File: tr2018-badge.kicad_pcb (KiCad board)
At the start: 2 copper layers, 70.4 x 53.3 mm, 23 parts, among them J1 Conn_01x02, J2 Conn_01x02, SW1 SW_SPDT, SW3 SW_Push, SW4 SW_Push, SW5 (opt.) SW_SPDT, U1 ESP-12F (opt.), X1 Defcon Shitty AddOn (opt.) >

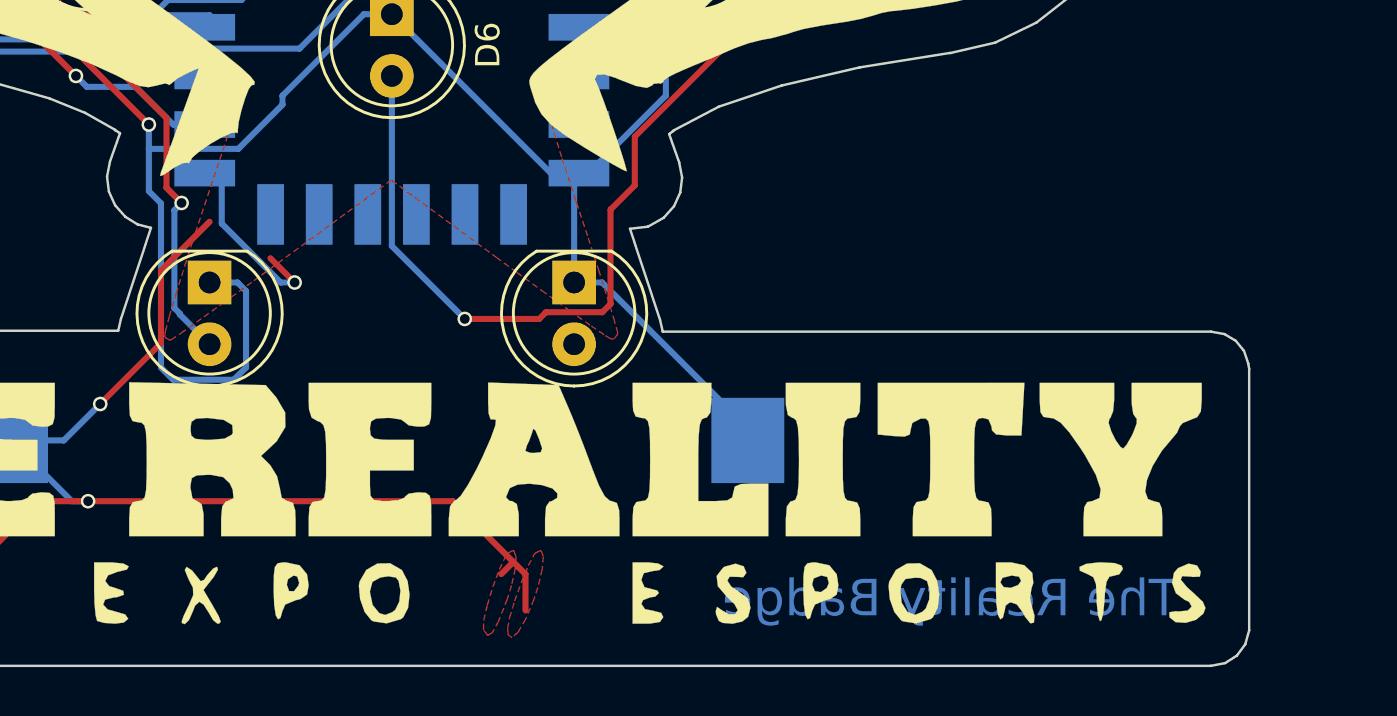
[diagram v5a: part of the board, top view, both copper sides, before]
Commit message: Made power bus more robust against edge cut errors
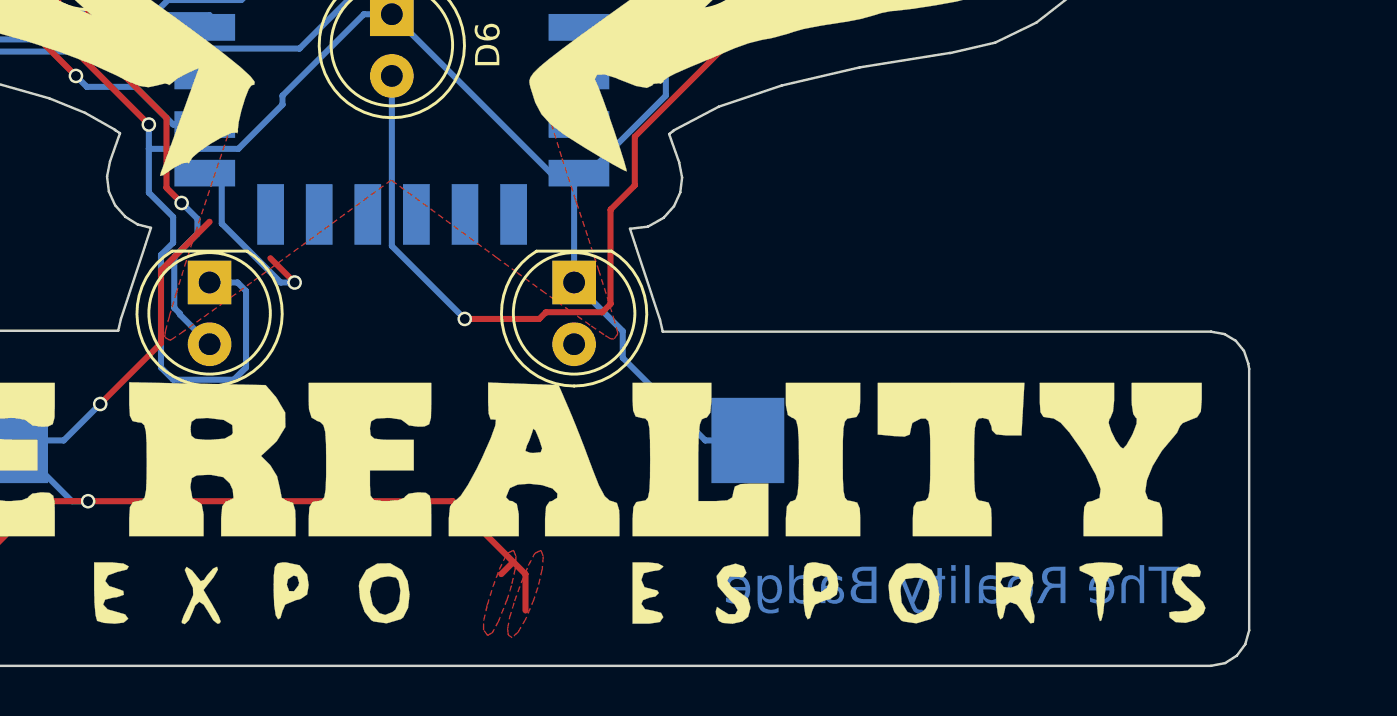
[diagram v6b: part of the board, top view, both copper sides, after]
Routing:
- net VCC: track 132.3 -> 134.2 mm
- net Net-(D1-Pad2): track 76.8 -> 77.3 mm
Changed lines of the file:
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@@
     (thickness 1.6)
     (drawings 173)
-    (tracks 248)
+    (tracks 254)
     (zones 0)
     (modules 23)
@@
     (pad_drill 0.762)
     (pad_to_mask_clearance 0.2)
-    (aux_axis_origin 111 122)
+    (aux_axis_origin 112 120.75)
     (visible_elements 7FFFFFFF)
     (pcbplotparams
@@
       (net 2 GND))
   )
-  (gr_text "The Reality Badge" (at 170 118) (layer B.Mask)
+  (gr_text "The Reality Badge" (at 170 117.5) (layer B.Mask)
     (effects (font (size 1.5 1.5) (thickness 0.3)) (justify mirror))
   )
-  (gr_text "The Reality Badge" (at 170 118) (layer B.Cu)
+  (gr_text "The Reality Badge" (at 170 117.5) (layer B.Cu)
     (effects (font (size 1.5 1.5) (thickness 0.3)) (justify mirror))
   )
@@
   (gr_line (start 180.968343 67.714581) (end 180.30263 67.523122) (layer Edge.Cuts) (width 0.1))
   (gr_line (start 181.118231 67.789525) (end 180.968343 67.714581) (layer Edge.Cuts) (width 0.1))
-  (segment (start 137 99.5) (end 137 101.243216) (width 0.25) (layer B.Cu) (net 1))
-  (segment (start 140.65 105) (end 139.5 105) (width 0.25) (layer B.Cu) (net 1))
-  (segment (start 137 101.243216) (end 137.5 101.743216) (width 0.25) (layer B.Cu) (net 1))
+  (segment (start 137 99.5) (end 137 101.303372) (width 0.25) (layer B.Cu) (net 1))
+  (segment (start 137 101.303372) (end 138 102.303372) (width 0.25) (layer B.Cu) (net 1))
+  (segment (start 138 102.303372) (end 138 103.36359) (width 0.25) (layer B.Cu) (net 1))
+  (segment (start 138 103.36359) (end 137.5 103.86359) (width 0.25) (layer B.Cu) (net 1))
+  (segment (start 137.5 103.86359) (end 137.5 108.5) (width 0.25) (layer B.Cu) (net 1))
+  (segment (start 138 109) (end 140.5 109) (width 0.25) (layer B.Cu) (net 1))
   (segment (start 137.5 108.5) (end 138 109) (width 0.25) (layer B.Cu) (net 1))
-  (segment (start 137.5 101.743216) (end 137.5 108.5) (width 0.25) (layer B.Cu) (net 1))
-  (segment (start 138 109) (end 140.5 109) (width 0.25) (layer B.Cu) (net 1))
   (segment (start 140.5 109) (end 141 108.5) (width 0.25) (layer B.Cu) (net 1))
   (segment (start 141 108.5) (end 141 105.35) (width 0.25) (layer B.Cu) (net 1))
   (segment (start 141 105.35) (end 140.65 105) (width 0.25) (layer B.Cu) (net 1))
+  (segment (start 140.65 105) (end 139.5 105) (width 0.25) (layer B.Cu) (net 1))
+  (segment (start 156.5 107) (end 154.5 105) (width 0.25) (layer B.Cu) (net 1))
+  (segment (start 156.5 108.1) (end 156.5 107) (width 0.25) (layer B.Cu) (net 1))
+  (segment (start 161.65 111.5) (end 159.9 111.5) (width 0.25) (layer B.Cu) (net 1))
+  (segment (start 159.9 111.5) (end 156.5 108.1) (width 0.25) (layer B.Cu) (net 1))
   (segment (start 117.96 81) (end 116.784999 82.175001) (width 0.25) (layer B.Cu) (net 1))
   (segment (start 116.784999 82.175001) (end 116.784999 86.420001) (width 0.25) (layer B.Cu) (net 1))
@@
   (segment (start 154.5 101) (end 154 100.5) (width 0.25) (layer B.Cu) (net 1))
   (segment (start 161.18 111.5) (end 161.18 110.53) (width 0.25) (layer B.Cu) (net 1))
-  (segment (start 161.18 110.53) (end 155.65 105) (width 0.25) (layer B.Cu) (net 1))
-  (segment (start 155.65 105) (end 154.5 105) (width 0.25) (layer B.Cu) (net 1))
   (segment (start 126.077476 76.948726) (end 126.077476 79.077476) (width 0.25) (layer F.Cu) (net 2))
   (segment (start 134.5 87.5) (end 136 89) (width 0.25) (layer F.Cu) (net 2))
@@
   (segment (start 139.5 107.54) (end 138.274999 106.314999) (width 0.25) (layer B.Cu) (net 12))
   (segment (start 138.274999 106.314999) (end 138.274999 106.274999) (width 0.25) (layer B.Cu) (net 12))
+  (segment (start 139 103) (end 139 102.37837) (width 0.25) (layer B.Cu) (net 12))
   (segment (start 138.274999 106.274999) (end 138.048646 106.048646) (width 0.25) (layer B.Cu) (net 12))
-  (segment (start 138.048646 106.048646) (end 138.048646 102.027014) (width 0.25) (layer B.Cu) (net 12))
-  (segment (start 138.048646 102.027014) (end 138.348645 101.727015) (width 0.25) (layer B.Cu) (net 12))
+  (segment (start 139 102.37837) (end 138.348645 101.727015) (width 0.25) (layer B.Cu) (net 12))
+  (segment (start 138.048646 106.048646) (end 138.048646 103.951354) (width 0.25) (layer B.Cu) (net 12))
+  (segment (start 138.048646 103.951354) (end 139 103) (width 0.25) (layer B.Cu) (net 12))
   (segment (start 129.620794 80.5) (end 136 86.879206) (width 0.25) (layer B.Cu) (net 12))
   (segment (start 127.119613 79.119613) (end 128.5 80.5) (width 0.25) (layer B.Cu) (net 12))

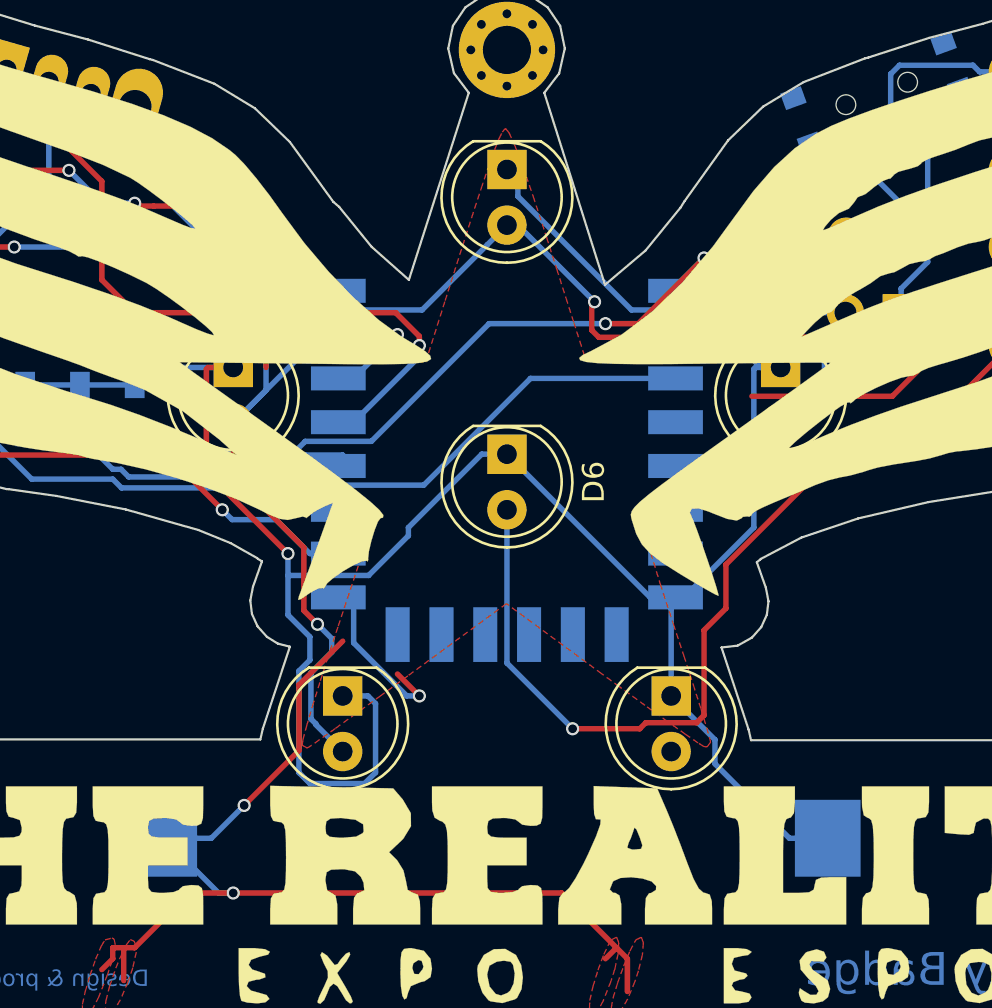
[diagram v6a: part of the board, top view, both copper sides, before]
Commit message: Added descriptive texts, fixed LED orientation, generated gerbers
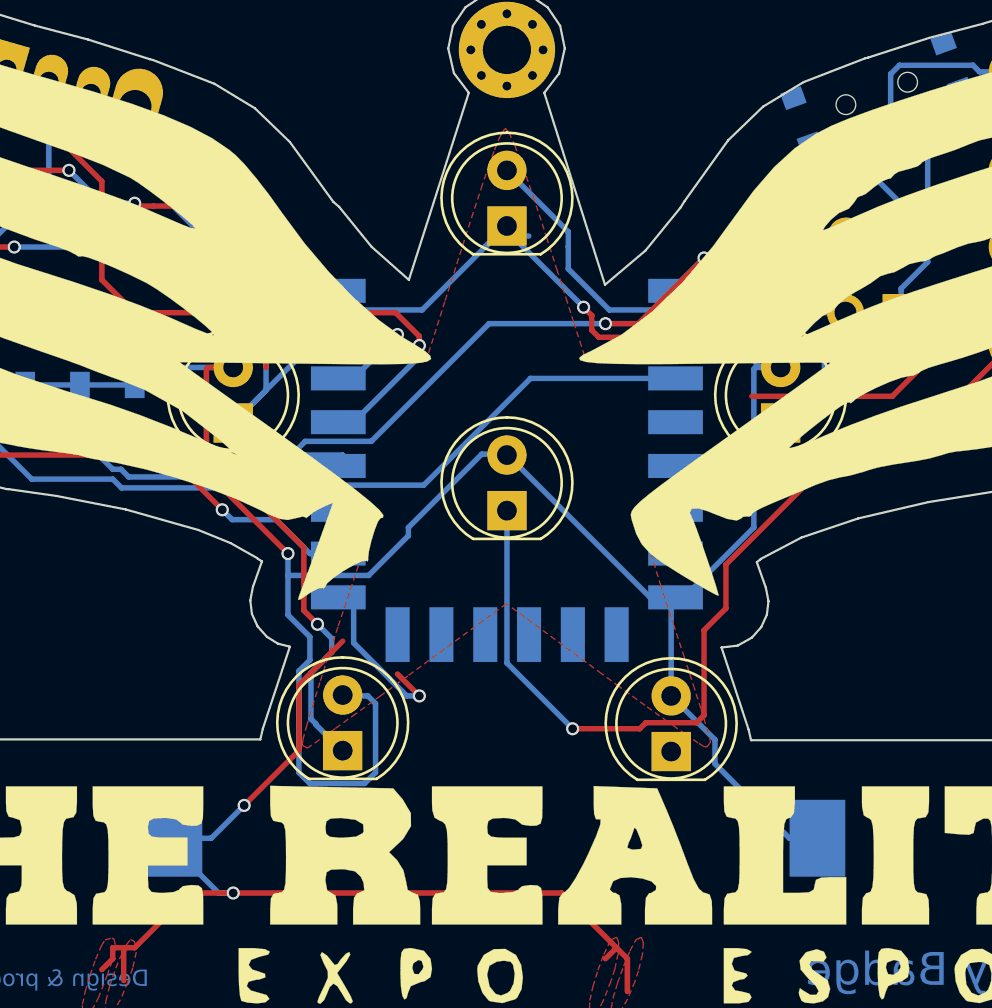
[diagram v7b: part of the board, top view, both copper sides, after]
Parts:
- removed D6: LED, LEDs:LED_D5.0mm
- added D6 (opt.): LED, LEDs:LED_D5.0mm, F.Cu at (147.0, 96.5)
- BT1: footprint BatteryHolder:Keystone_1058_1x2032-CoinCell -> Battery_Holders:Keystone_1058_1x2032-CoinCell
- R5: value 10k (all opt.) -> All 10k (opt.)
- U1: value ESP-12F (opt.) -> ESP8266 (opt.)
- moved D1 2.58 mm to (147.0, 83.5), turned to 90 degrees
- moved D2 2.54 mm to (159.5, 92.5), turned to 90 degrees
- moved D3 2.54 mm to (154.5, 107.5), turned to 90 degrees
- moved D5 2.54 mm to (134.5, 92.5), turned to 90 degrees
- moved D4 2.50 mm to (139.5, 107.5), turned to 90 degrees
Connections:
- D1 pad 1: VCC -> Net-(D1-Pad1)
- D1 pad 2: Net-(D1-Pad2) -> VCC
- D2 pad 1: VCC -> Net-(D1-Pad1)
- D2 pad 2: Net-(D1-Pad2) -> VCC
- D3 pad 1: VCC -> Net-(D1-Pad1)
- D3 pad 2: Net-(D1-Pad2) -> VCC
- D4 pad 1: VCC -> Net-(D1-Pad1)
- D4 pad 2: Net-(D1-Pad2) -> VCC
- D5 pad 1: VCC -> Net-(D1-Pad1)
- D5 pad 2: Net-(D1-Pad2) -> VCC
- SW1 pad 3: Net-(D1-Pad2) -> Net-(D1-Pad1)
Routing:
- net Net-(D1-Pad1): track 0.00 -> 79.6 mm, vias 0 -> 3
- net Net-(D1-Pad2): track 77.3 -> 0.00 mm, vias 3 -> 0
- net VCC: track 134.2 -> 135.5 mm
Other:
- board text added: "3V3 (+)"
- board text added: "ESP allows I2C comm. for Shitty AddOn"
- board text added: "GND (-)"
- board text added: "SW1 powers D1-5"
- board text added: "SW3 powers D6"
- board text added: "SW5 selects whether SW4 powers J1 or J2"
- board text added: "|GND 3V3|"
